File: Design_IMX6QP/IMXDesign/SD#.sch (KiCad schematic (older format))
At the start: 1 part, among them U1 MCIMX6QP5EVT

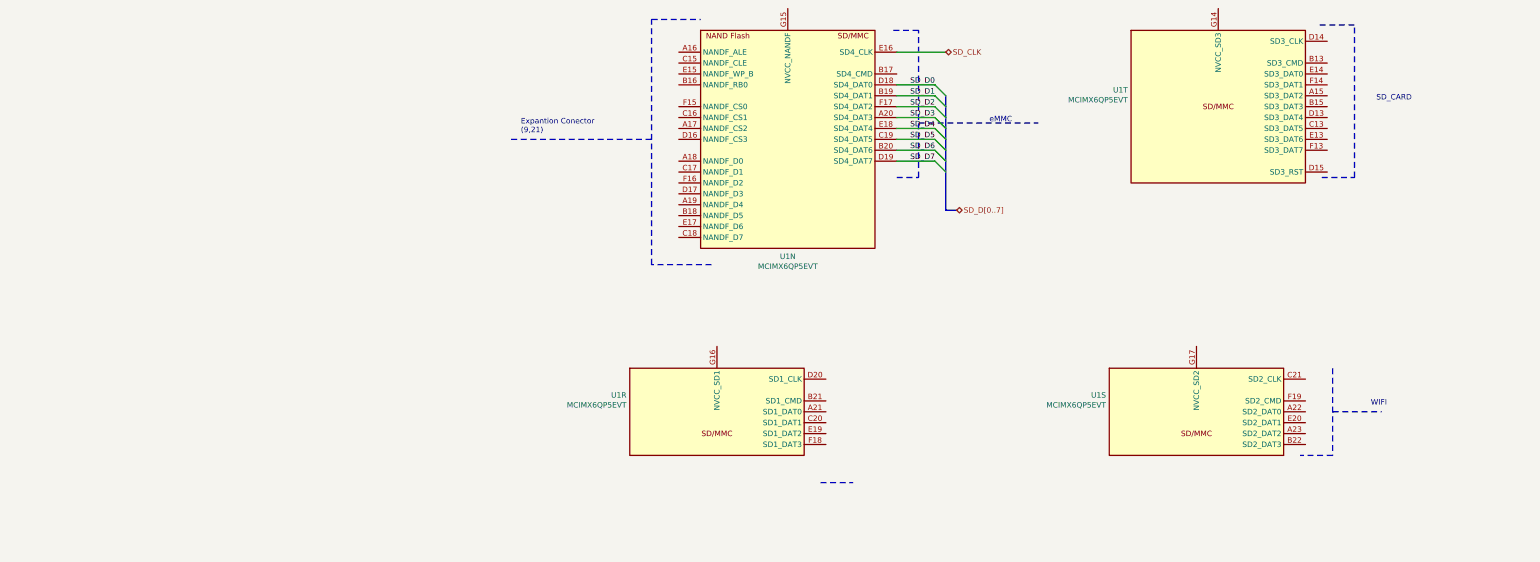
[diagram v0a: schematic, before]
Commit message: Update IMX6QP and IMX8MQ
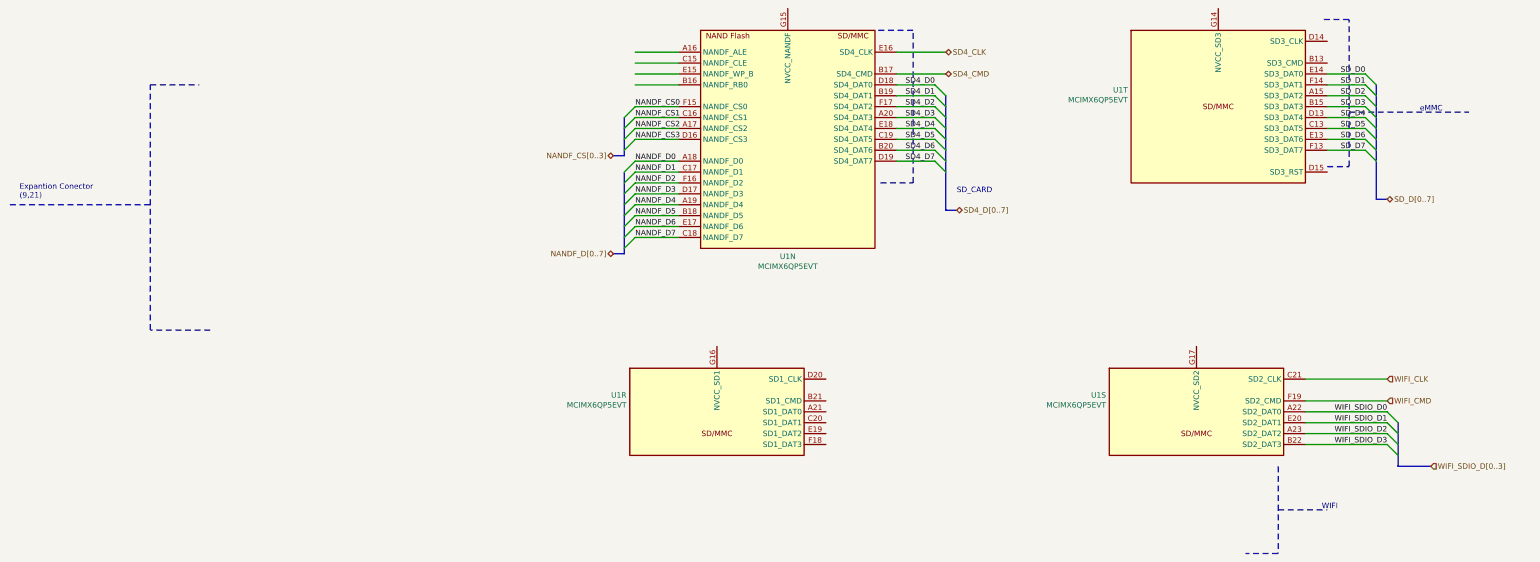
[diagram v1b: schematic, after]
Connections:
- net labels added: NANDF_CS0, NANDF_CS1, NANDF_CS2, NANDF_CS3, NANDF_CS[0..3], NANDF_D0, NANDF_D1, NANDF_D2, NANDF_D3, NANDF_D4, NANDF_D5, NANDF_D6, NANDF_D7, NANDF_D[0..7], SD4_CLK, SD4_CMD, SD4_D0, SD4_D1, SD4_D2, SD4_D3, SD4_D4, SD4_D5, SD4_D6, SD4_D7, SD4_D[0..7], WIFI_CLK, WIFI_CMD, WIFI_SDIO_D0, WIFI_SDIO_D1, WIFI_SDIO_D2, WIFI_SDIO_D3, WIFI_SDIO_D[0..3]
- net labels removed: SD_CLK
- wire segments 9 -> 40
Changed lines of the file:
@@
 $Descr A4 11693 8268
 encoding utf-8
-Sheet 7 12
+Sheet 13 17
 Title ""
 Date ""
@@
 Comment4 ""
 $EndDescr
-Wire Notes Line
-	5400 1550 5150 1550
-Text Notes 1750 2500 0    50   ~ 0
+Text Notes -2850 3100 0    50   ~ 0
 Expantion Conector \n(9,21)
 Wire Notes Line
-	2950 2550 1650 2550
-Wire Notes Line
-	2950 1450 3400 1450
-Wire Notes Line
-	2950 3700 2950 1450
-Wire Notes Line
-	3500 3700 2950 3700
-$Comp
-L CPU_NXP_IMX:MCIMX6QP5EVT U?
-U 14 1 60D9B7A4
-P 4200 2550
-AR Path="/60D9B7A4" Ref="U?"  Part="14"
-AR Path="/61E20C73/60D9B7A4" Ref="U?"  Part="14"
-AR Path="/61E20C73/60D2D67D/60D9B7A4" Ref="U1"  Part="14"
-F 0 "U1" H 4200 1475 50  0000 C CNN
-F 1 "MCIMX6QP5EVT" H 4200 1384 50  0000 C CNN
-F 2 "Package_BGA:BGA-624_21.0x21.0mm_Layout25x25_P0.8mm" H 3650 4750 50  0001 C CNN
-F 3 "https://www.nxp.com/docs/en/data-sheet/IMX6DQPCEC.pdf" H 3750 4750 50  0001 C CNN
-	14   4200 2550
-	1    0    0    -1
-$EndComp
+	-1650 3150 -2950 3150
+Wire Notes Line
+	-1650 2050 -1200 2050
+Wire Notes Line
+	-1650 4300 -1650 2050
+Wire Notes Line
+	-1100 4300 -1650 4300
 Wire Wire Line
 	5200 1750 5650 1750
 Text HLabel 5650 1750 2    50   BiDi ~ 0
-SD_CLK
-Text Label 5550 2750 2    50   ~ 0
-SD_D7
-Text Label 5550 2650 2    50   ~ 0
-SD_D6
-Text Label 5550 2550 2    50   ~ 0
-SD_D5
-Text Label 5550 2450 2    50   ~ 0
-SD_D4
-Text Label 5550 2350 2    50   ~ 0
-SD_D3
-Text Label 5550 2250 2    50   ~ 0
-SD_D2
-Text Label 5550 2150 2    50   ~ 0
-SD_D1
-Text Label 5550 2050 2    50   ~ 0
-SD_D0
-Wire Wire Line
-	5200 2750 5550 2750
-Entry Wire Line
-	5550 2750 5650 2850
-Wire Wire Line
-	5200 2650 5550 2650
-Entry Wire Line
-	5550 2650 5650 2750
-Wire Wire Line
-	5200 2550 5550 2550
-Entry Wire Line
-	5550 2550 5650 2650
-Wire Wire Line
-	5200 2450 5550 2450
-Entry Wire Line
-	5550 2450 5650 2550
-Wire Wire Line
-	5200 2350 5550 2350
-Entry Wire Line
-	5550 2350 5650 2450
-Wire Wire Line
-	5200 2250 5550 2250
-Entry Wire Line
-	5550 2250 5650 2350
-Wire Wire Line
-	5200 2150 5550 2150
-Entry Wire Line
-	5550 2150 5650 2250
-Wire Wire Line
-	5200 2050 5550 2050
-Entry Wire Line
-	5550 2050 5650 2150
-Text HLabel 5750 3200 2    50   BiDi ~ 0
-SD_D[0..7]
-Wire Bus Line
-	5650 3200 5750 3200
-Wire Notes Line
-	5200 2900 5400 2900
-Wire Notes Line
-	5400 2900 5400 1550
-Wire Notes Line
-	5400 2400 6500 2400
-Text Notes 6050 2400 0    50   ~ 0
-eMMC
+SD4_CLK
 $Comp
 L CPU_NXP_IMX:MCIMX6QP5EVT U?
@@
 	1    0    0    -1
 $EndComp
-Wire Notes Line
-	4500 5700 4800 5700
-Wire Notes Line
-	9200 4650 9200 5450
-Wire Notes Line
-	9200 5450 8900 5450
-Wire Notes Line
-	9200 5050 9650 5050
-Text Notes 9550 5000 0    50   ~ 0
+Text Notes 9100 5950 0    50   ~ 0
 WIFI
-Text Notes 9600 2200 0    50   ~ 0
+Text Notes 5750 3050 0    50   ~ 0
 SD_CARD
 Wire Notes Line
-	9100 2900 9400 2900
-Wire Notes Line
-	9400 2900 9400 1500
-Wire Notes Line
-	9400 1500 9050 1500
+	5050 2950 5350 2950
+Wire Notes Line
+	5350 2950 5350 1550
+Wire Notes Line
+	5350 1550 5000 1550
+Wire Notes Line
+	8700 5950 9150 5950
+Wire Notes Line
+	8700 6350 8400 6350
+Wire Notes Line
+	8700 5550 8700 6350
+Wire Wire Line
+	8950 5350 9700 5350
+Wire Wire Line
+	8950 4950 9700 4950
+Wire Wire Line
+	8950 4750 9700 4750
+Entry Wire Line
+	9700 5350 9800 5450
+Entry Wire Line
+	9700 5250 9800 5350
+Entry Wire Line
+	9700 5150 9800 5250
+Entry Wire Line
+	9700 5050 9800 5150
+Wire Bus Line
+	9800 5550 10100 5550
+Text HLabel 10100 5550 2    50   Input ~ 0
+WIFI_SDIO_D[0..3]
+Text Label 9700 5350 2    50   ~ 0
+WIFI_SDIO_D3
+Wire Wire Line
+	8950 5250 9700 5250
+Text Label 9700 5250 2    50   ~ 0
+WIFI_SDIO_D2
+Wire Wire Line
+	8950 5150 9700 5150
+Text Label 9700 5150 2    50   ~ 0
+WIFI_SDIO_D1
+Wire Wire Line
+	8950 5050 9700 5050
+Text Label 9700 5050 2    50   ~ 0
+WIFI_SDIO_D0
+Text HLabel 9700 4750 2    50   Input ~ 0
+WIFI_CLK
+Text HLabel 9700 4950 2    50   Input ~ 0
+WIFI_CMD
+$Comp
+L CPU_NXP_IMX:MCIMX6QP5EVT U?
+U 14 1 60D9B7A4
+P 4200 2550
+AR Path="/60D9B7A4" Ref="U?"  Part="14"
+AR Path="/61E20C73/60D9B7A4" Ref="U?"  Part="14"
+AR Path="/61E20C73/60D2D67D/60D9B7A4" Ref="U1"  Part="14"
+F 0 "U1" H 4200 1475 50  0000 C CNN
+F 1 "MCIMX6QP5EVT" H 4200 1384 50  0000 C CNN
+F 2 "Package_BGA:BGA-624_21.0x21.0mm_Layout25x25_P0.8mm" H 3650 4750 50  0001 C CNN
+F 3 "https://www.nxp.com/docs/en/data-sheet/IMX6DQPCEC.pdf" H 3750 4750 50  0001 C CNN
+	14   4200 2550
+	1    0    0    -1
+$EndComp
+Wire Notes Line
+	9350 1450 9100 1450
+Text Notes 10000 2300 0    50   ~ 0
+eMMC
+Wire Notes Line
+	9350 2300 10450 2300
+Wire Notes Line
+	9350 2800 9350 1450
+Wire Notes Line
+	9150 2800 9350 2800
+Wire Bus Line
+	9600 3100 9700 3100
+Text HLabel 9700 3100 2    50   BiDi ~ 0
+SD_D[0..7]
+Entry Wire Line
+	9500 1950 9600 2050
+Wire Wire Line
+	9150 1950 9500 1950
+Entry Wire Line
+	9500 2050 9600 2150
+Wire Wire Line
+	9150 2050 9500 2050
+Entry Wire Line
+	9500 2150 9600 2250
+Wire Wire Line
+	9150 2150 9500 2150
+Entry Wire Line
+	9500 2250 9600 2350
+Wire Wire Line
+	9150 2250 9500 2250
+Entry Wire Line
+	9500 2350 9600 2450
+Wire Wire Line
+	9150 2350 9500 2350
+Entry Wire Line
+	9500 2450 9600 2550
+Wire Wire Line
+	9150 2450 9500 2450
+Entry Wire Line
+	9500 2550 9600 2650
+Wire Wire Line
+	9150 2550 9500 2550
+Entry Wire Line
+	9500 2650 9600 2750
+Wire Wire Line
+	9150 2650 9500 2650
+Text Label 9500 1950 2    50   ~ 0
+SD_D0
+Text Label 9500 2050 2    50   ~ 0
+SD_D1
+Text Label 9500 2150 2    50   ~ 0
+SD_D2
+Text Label 9500 2250 2    50   ~ 0
+SD_D3
+Text Label 9500 2350 2    50   ~ 0
+SD_D4
+Text Label 9500 2450 2    50   ~ 0
+SD_D5
+Text Label 9500 2550 2    50   ~ 0
+SD_D6
+Text Label 9500 2650 2    50   ~ 0
+SD_D7
+Wire Bus Line
+	5650 3200 5750 3200
+Text HLabel 5750 3200 2    50   BiDi ~ 0
+SD4_D[0..7]
+Entry Wire Line
+	5550 2050 5650 2150
+Wire Wire Line
+	5200 2050 5550 2050
+Entry Wire Line
+	5550 2150 5650 2250
+Wire Wire Line
+	5200 2150 5550 2150
+Entry Wire Line
+	5550 2250 5650 2350
+Wire Wire Line
+	5200 2250 5550 2250
+Entry Wire Line
+	5550 2350 5650 2450
+Wire Wire Line
+	5200 2350 5550 2350
+Entry Wire Line
+	5550 2450 5650 2550
+Wire Wire Line
+	5200 2450 5550 2450
+Entry Wire Line
+	5550 2550 5650 2650
+Wire Wire Line
+	5200 2550 5550 2550
+Entry Wire Line
+	5550 2650 5650 2750
+Wire Wire Line
+	5200 2650 5550 2650
+Entry Wire Line
+	5550 2750 5650 2850
+Wire Wire Line
+	5200 2750 5550 2750
+Text Label 5550 2050 2    50   ~ 0
+SD4_D0
+Text Label 5550 2150 2    50   ~ 0
+SD4_D1
+Text Label 5550 2250 2    50   ~ 0
+SD4_D2
+Text Label 5550 2350 2    50   ~ 0
+SD4_D3
+Text Label 5550 2450 2    50   ~ 0
+SD4_D4
+Text Label 5550 2550 2    50   ~ 0
+SD4_D5
+Text Label 5550 2650 2    50   ~ 0
+SD4_D6
+Text Label 5550 2750 2    50   ~ 0
+SD4_D7
+Wire Wire Line
+	5200 1950 5650 1950
+Text HLabel 5650 1950 2    50   BiDi ~ 0
+SD4_CMD
+Wire Bus Line
+	2700 3600 2600 3600
+Entry Wire Line
+	2800 2750 2700 2850
+Entry Wire Line
+	2800 2850 2700 2950
+Entry Wire Line
+	2800 2950 2700 3050
+Entry Wire Line
+	2800 3050 2700 3150
+Entry Wire Line
+	2800 3150 2700 3250
+Entry Wire Line
+	2800 3250 2700 3350
+Entry Wire Line
+	2800 3350 2700 3450
+Entry Wire Line
+	2800 3450 2700 3550
+Text Label 2800 2750 0    50   ~ 0
+NANDF_D0
+Text Label 2800 2850 0    50   ~ 0
+NANDF_D1
+Text Label 2800 2950 0    50   ~ 0
+NANDF_D2
+Text Label 2800 3050 0    50   ~ 0
+NANDF_D3
+Text Label 2800 3150 0    50   ~ 0
+NANDF_D4
+Text Label 2800 3250 0    50   ~ 0
+NANDF_D5
+Text Label 2800 3350 0    50   ~ 0
+NANDF_D6
+Text Label 2800 3450 0    50   ~ 0
+NANDF_D7
+Text HLabel 2600 3600 0    50   BiDi ~ 0
+NANDF_D[0..7]
+Wire Wire Line
+	2800 2750 3200 2750
+Wire Wire Line
+	3200 2850 2800 2850
+Wire Wire Line
+	3200 2950 2800 2950
+Wire Wire Line
+	3200 3050 2800 3050
+Wire Wire Line
+	3200 3150 2800 3150
+Wire Wire Line
+	3200 3250 2800 3250
+Wire Wire Line
+	3200 3350 2800 3350
+Wire Wire Line
+	3200 3450 2800 3450
+Wire Bus Line
+	2700 2700 2600 2700
+Entry Wire Line
+	2800 2250 2700 2350
+Entry Wire Line
+	2800 2350 2700 2450
+Entry Wire Line
+	2800 2450 2700 2550
+Entry Wire Line
+	2800 2550 2700 2650
+Text Label 2800 2350 0    50   ~ 0
+NANDF_CS1
+Text Label 2800 2450 0    50   ~ 0
+NANDF_CS2
+Text Label 2800 2550 0    50   ~ 0
+NANDF_CS3
+Text HLabel 2600 2700 0    50   BiDi ~ 0
+NANDF_CS[0..3]
+Wire Wire Line
+	3200 2250 2800 2250
+Wire Wire Line
+	3200 2350 2800 2350
+Wire Wire Line
+	3200 2450 2800 2450
+Wire Wire Line
+	3200 2550 2800 2550
+Text Label 2800 2250 0    50   ~ 0
+NANDF_CS0
+Wire Wire Line
+	3200 1750 2800 1750
+Wire Wire Line
+	3200 1850 2800 1850
+Wire Wire Line
+	3200 1950 2800 1950
+Wire Wire Line
+	3200 2050 2800 2050
+Wire Bus Line
+	9800 5150 9800 5550
+Wire Bus Line
+	2700 2350 2700 2700
+Wire Bus Line
+	2700 2850 2700 3600
 Wire Bus Line
 	5650 2150 5650 3200
+Wire Bus Line
+	9600 2050 9600 3100
 $EndSCHEMATC
